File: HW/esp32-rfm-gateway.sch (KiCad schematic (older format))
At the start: 31 parts, among them J1 ph_1x2, J2 ph_1x2, J3 ph_1x3, J30 AntSMA, J4 ph_1x4, J5 ph_1x4, J6 ph_1x3, J7 ph_1x4, U1 ESP-WROOM-32, U2 BD48K30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

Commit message: Adds a new I2C connector, a LED for 5V indication, some SMD connections for a few free pins and labels
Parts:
- added J10, J11, J12, J13, J14: CS_1, CalinConnectors:SMD_Pins_1x1, symbol calin:CS_1
- added J8: ph_1x4, CalinConnectors:Pin_Header_Straight_1x04, symbol calin:CS_4
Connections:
- wire segments 134 -> 143
- no-connect marks 16 -> 12
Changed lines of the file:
@@
 Sheet 1 3
 Title "ESP32 RFM69/RFM9x Gateway"
-Date "2019-04-22"
-Rev "30"
+Date "2019-04-25"
+Rev "32"
 Comp "Calin Radoni"
 Comment1 ""
@@
 Connection ~ 5900 2900
 NoConn ~ 5900 1700
-NoConn ~ 5900 2300
-NoConn ~ 5900 2400
-NoConn ~ 5900 2500
 $Comp
 L calin:CS_5 J30
@@
 Text Label 7750 1400 0    50   ~ 0
 SDA
-NoConn ~ 5900 2800
 Text Label 5200 2800 0    50   ~ 0
 IO4
@@
 Text Label 8150 5150 0    50   ~ 0
 Reset
+$Comp
+L calin:CS_4 J8
+U 1 1 5CC3F23B
+P 9300 1250
+F 0 "J8" H 9300 1500 60  0000 C CNN
+F 1 "ph_1x4" V 9400 1250 50  0000 C CNN
+F 2 "CalinConnectors:Pin_Header_Straight_1x04" H 9300 1400 60  0001 C CNN
+F 3 "" H 9300 1400 60  0000 C CNN
+	1    9300 1250
+	1    0    0    -1
+$EndComp
+$Comp
+L power:GND #PWR0178
+U 1 1 5CC3F241
+P 9050 1200
+F 0 "#PWR0178" H 9050 950 50  0001 C CNN
+F 1 "GND" V 9050 1000 50  0000 C CNN
+F 2 "" H 9050 1200 50  0000 C CNN
+F 3 "" H 9050 1200 50  0000 C CNN
+	1    9050 1200
+	0    1    1    0
+$EndComp
+$Comp
+L power:+3V3 #PWR0179
+U 1 1 5CC3F247
+P 9050 1100
+F 0 "#PWR0179" H 9050 950 50  0001 C CNN
+F 1 "+3V3" V 9050 1300 50  0000 C CNN
+F 2 "" H 9050 1100 50  0000 C CNN
+F 3 "" H 9050 1100 50  0000 C CNN
+	1    9050 1100
+	0    -1   -1   0
+$EndComp
+Wire Wire Line
+	9150 1100 9050 1100
+Wire Wire Line
+	9150 1200 9050 1200
+Wire Wire Line
+	9150 1300 8650 1300
+Wire Wire Line
+	9150 1400 8650 1400
+Text Label 8750 1300 0    50   ~ 0
+SCL
+Text Label 8750 1400 0    50   ~ 0
+SDA
+$Comp
+L calin:CS_1 J10
+U 1 1 5CC44237
+P 9300 1900
+F 0 "J10" H 9400 1900 60  0000 L CNN
+F 1 "CS_1" H 9600 1900 50  0000 L CNN
+F 2 "CalinConnectors:SMD_Pins_1x1" H 9300 1900 60  0001 C CNN
+F 3 "" H 9300 1900 60  0000 C CNN
+	1    9300 1900
+	1    0    0    -1
+$EndComp
+$Comp
+L calin:CS_1 J11
+U 1 1 5CC442FF
+P 9300 2050
+F 0 "J11" H 9400 2050 60  0000 L CNN
+F 1 "CS_1" H 9600 2050 50  0000 L CNN
+F 2 "CalinConnectors:SMD_Pins_1x1" H 9300 2050 60  0001 C CNN
+F 3 "" H 9300 2050 60  0000 C CNN
+	1    9300 2050
+	1    0    0    -1
+$EndComp
+$Comp
+L calin:CS_1 J12
+U 1 1 5CC44353
+P 9300 2200
+F 0 "J12" H 9400 2200 60  0000 L CNN
+F 1 "CS_1" H 9600 2200 50  0000 L CNN
+F 2 "CalinConnectors:SMD_Pins_1x1" H 9300 2200 60  0001 C CNN
+F 3 "" H 9300 2200 60  0000 C CNN
+	1    9300 2200
+	1    0    0    -1
+$EndComp
+$Comp
+L calin:CS_1 J13
+U 1 1 5CC443A9
+P 9300 2350
+F 0 "J13" H 9400 2350 60  0000 L CNN
+F 1 "CS_1" H 9600 2350 50  0000 L CNN
+F 2 "CalinConnectors:SMD_Pins_1x1" H 9300 2350 60  0001 C CNN
+F 3 "" H 9300 2350 60  0000 C CNN
+	1    9300 2350
+	1    0    0    -1
+$EndComp
+$Comp
+L calin:CS_1 J14
+U 1 1 5CC44401
+P 9300 2500
+F 0 "J14" H 9400 2500 60  0000 L CNN
+F 1 "CS_1" H 9600 2500 50  0000 L CNN
+F 2 "CalinConnectors:SMD_Pins_1x1" H 9300 2500 60  0001 C CNN
+F 3 "" H 9300 2500 60  0000 C CNN
+	1    9300 2500
+	1    0    0    -1
+$EndComp
+Wire Wire Line
+	9150 1900 8650 1900
+Wire Wire Line
+	9150 2050 8650 2050
+Wire Wire Line
+	9150 2200 8650 2200
+Wire Wire Line
+	9150 2500 8650 2500
+$Comp
+L power:GND #PWR0180
+U 1 1 5CC64F5B
+P 9050 2350
+F 0 "#PWR0180" H 9050 2100 50  0001 C CNN
+F 1 "GND" V 9050 2150 50  0000 C CNN
+F 2 "" H 9050 2350 50  0000 C CNN
+F 3 "" H 9050 2350 50  0000 C CNN
+	1    9050 2350
+	0    1    1    0
+$EndComp
+Wire Wire Line
+	9150 2350 9050 2350
+Text Label 8750 2500 0    50   ~ 0
+IO4
+Text Label 8750 2200 0    50   ~ 0
+IO5
+Text Label 8750 2050 0    50   ~ 0
+IO18
+Text Label 8750 1900 0    50   ~ 0
+IO19
 $EndSCHEMATC

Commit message: Updates components to add manufacturer, part number, ... fields. Also checked some values.
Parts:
- C1, C2, C30, C32, C4, C5, C6: symbol Device:C -> calin:C; characteristics (none) -> 100 nF / 50V / X7R; manufacturer (none) -> Samsung; package (none) -> 0805; part-number (none) -> CL21B104KBCNNNC
- C3, C31: symbol Device:C -> calin:C; characteristics (none) -> 10 µF / 6,3 V; manufacturer (none) -> Samsung; package (none) -> 0805; part-number (none) -> CL21B106KQQNNNE
- H1, H2, H3, H4, J10, J11, J12, J13, J14: Notes (none) -> DNP; Variant (none) -> pcb
- J1, J2, J7: Notes (none) -> DNP; Variant (none) -> test
- R1: characteristics (none) -> 10k; manufacturer (none) -> Vishay; package (none) -> 0805; part-number (none) -> CRCW080510K0FKEA
- R2: characteristics (none) -> 330; manufacturer (none) -> Vishay; package (none) -> 0805; part-number (none) -> CRCW0805330RFKTABC
- R3, R4: characteristics (none) -> 2k; manufacturer (none) -> Panasonic; package (none) -> 0805; part-number (none) -> ERJ6ENF2001V
- SYM2, SYM5: Notes (none) -> DNP; Variant (none) -> pcb; part-number (none) -> DNP
- U1: characteristics (none) -> *; manufacturer (none) -> Espressif; package (none) -> *; part-number (none) -> ESP32-WROOM-32
- U2: Notes (none) -> DNP; Variant (none) -> test; characteristics (none) -> Standard CMOS Voltage Detector IC 3.0V; manufacturer (none) -> ROHM Semiconductor; package (none) -> SSOP3 (SOT23-3); part-number (none) -> BD49K30
- U30: characteristics (none) -> *; manufacturer (none) -> HOPERF; package (none) -> *; part-number (none) -> RFM69HCW

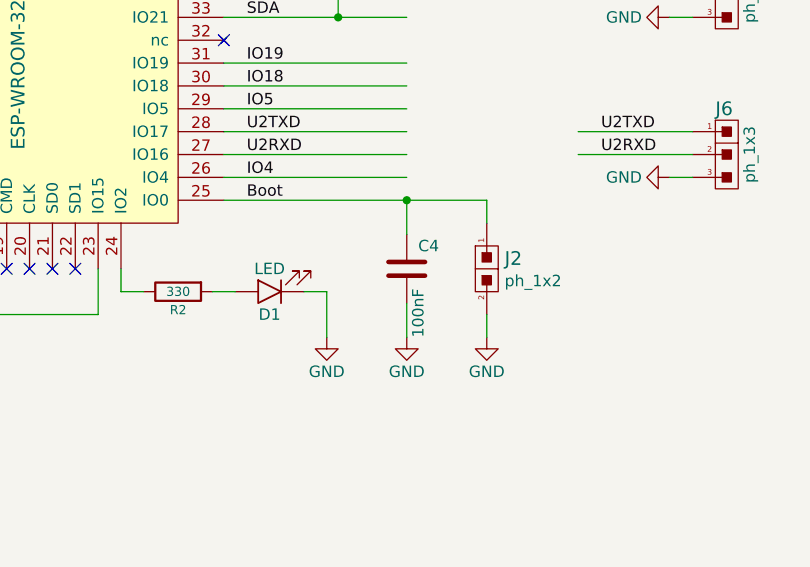
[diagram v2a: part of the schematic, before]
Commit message: Changes C4 to NC to prevent unwanted boot to Download mode and removes keepout area from under the ESP32 module.
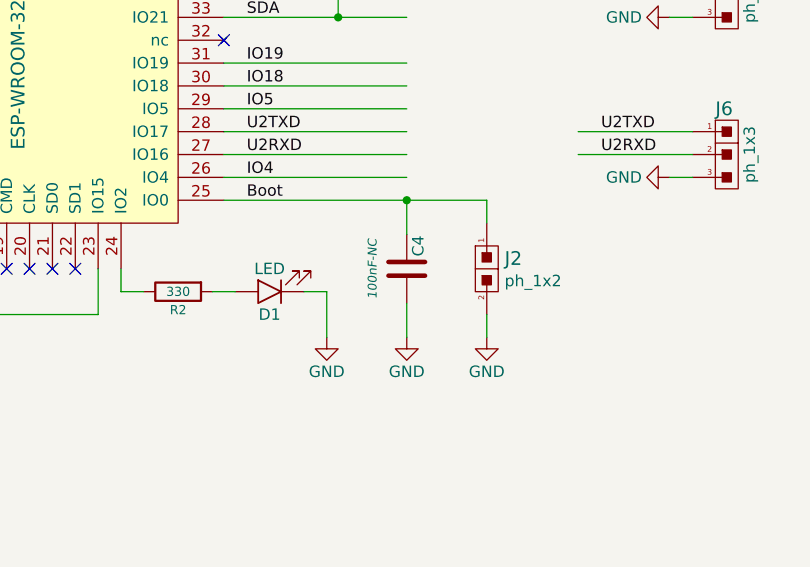
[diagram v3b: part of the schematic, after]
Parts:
- C4: value 100nF -> 100nF-NC; characteristics 100 nF / 50V / X7R -> *; manufacturer Samsung -> *; part-number CL21B104KBCNNNC -> DNP
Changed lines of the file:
@@
 Title "ESP32 RFM69/RFM9x Gateway"
 Date "2019-05-02"
-Rev "33"
+Rev "34"
 Comp "Calin Radoni"
 Comment1 ""
@@
 U 1 1 5B37F59B
 P 5900 3200
-F 0 "C4" H 5950 3300 50  0000 L CNN
-F 1 "100nF" V 5950 2900 50  0000 L CNN
+F 0 "C4" V 5950 3300 50  0000 C CNN
+F 1 "100nF-NC" V 5750 3200 39  0000 C CIN
 F 2 "CalinGeneric:C0805HS" H 5938 3050 50  0001 C CNN
 F 3 "" H 5900 3200 50  0000 C CNN
-F 4 "100 nF / 50V / X7R" H 0   0   50  0001 C CNN "characteristics"
-F 5 "Samsung" H 0   0   50  0001 C CNN "manufacturer"
+F 4 "*" H 0   0   50  0001 C CNN "characteristics"
+F 5 "*" H 0   0   50  0001 C CNN "manufacturer"
 F 6 "0805" H 0   0   50  0001 C CNN "package"
-F 7 "CL21B104KBCNNNC" H 0   0   50  0001 C CNN "part-number"
+F 7 "DNP" H 0   0   50  0001 C CNN "part-number"
 	1    5900 3200
 	1    0    0    -1

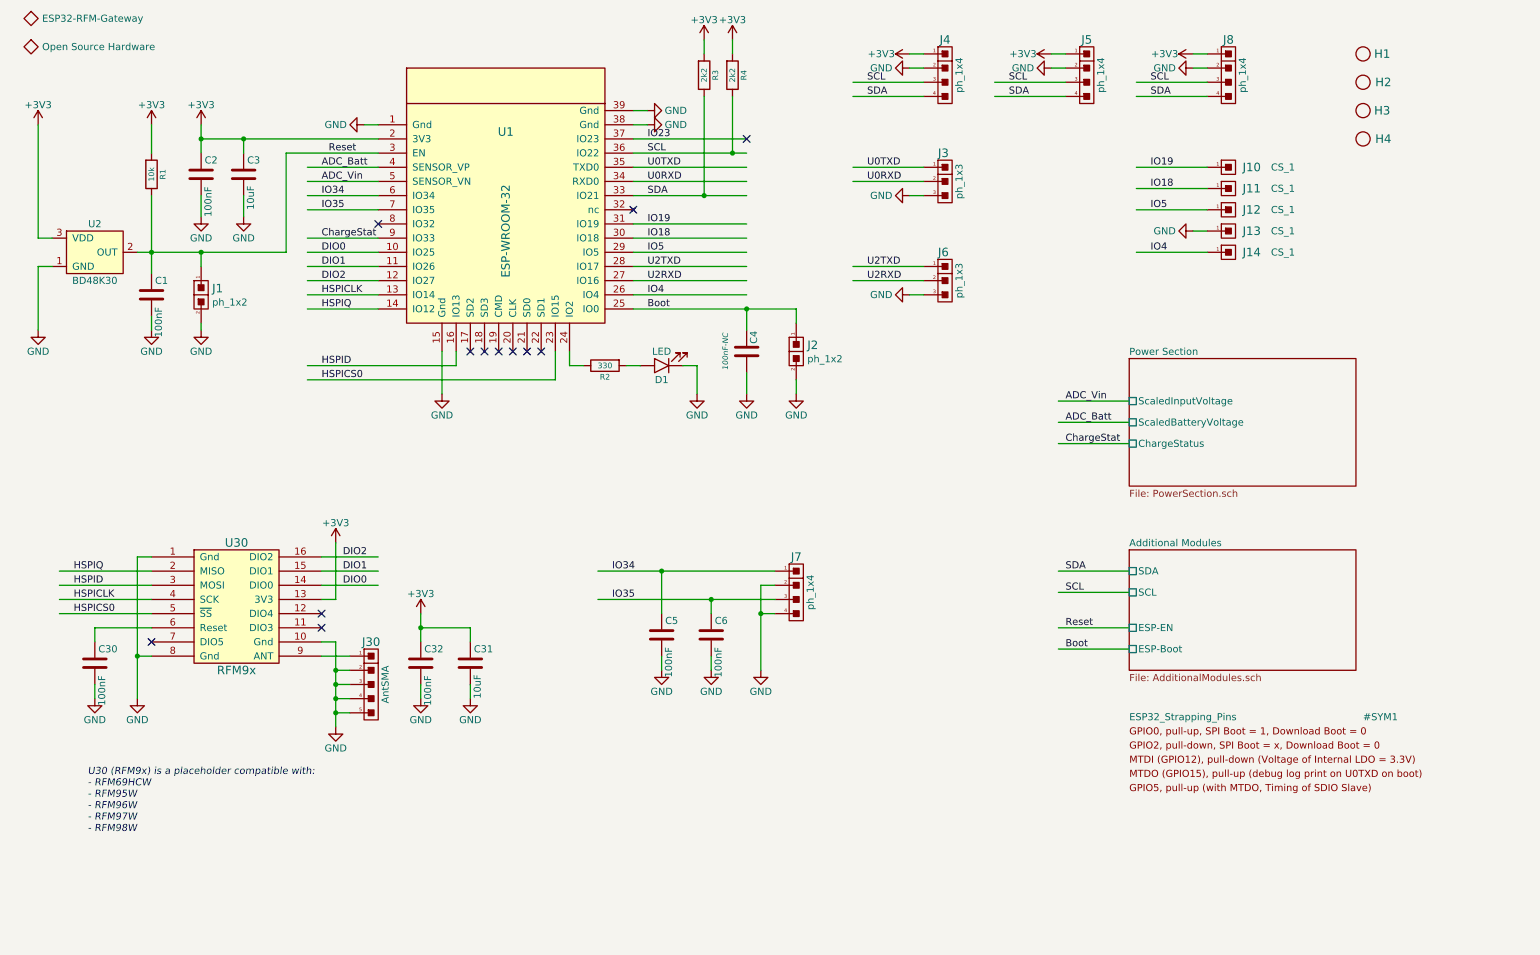
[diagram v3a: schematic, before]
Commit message: Connects the LEDs straight to ESP32, removing the LED driver.
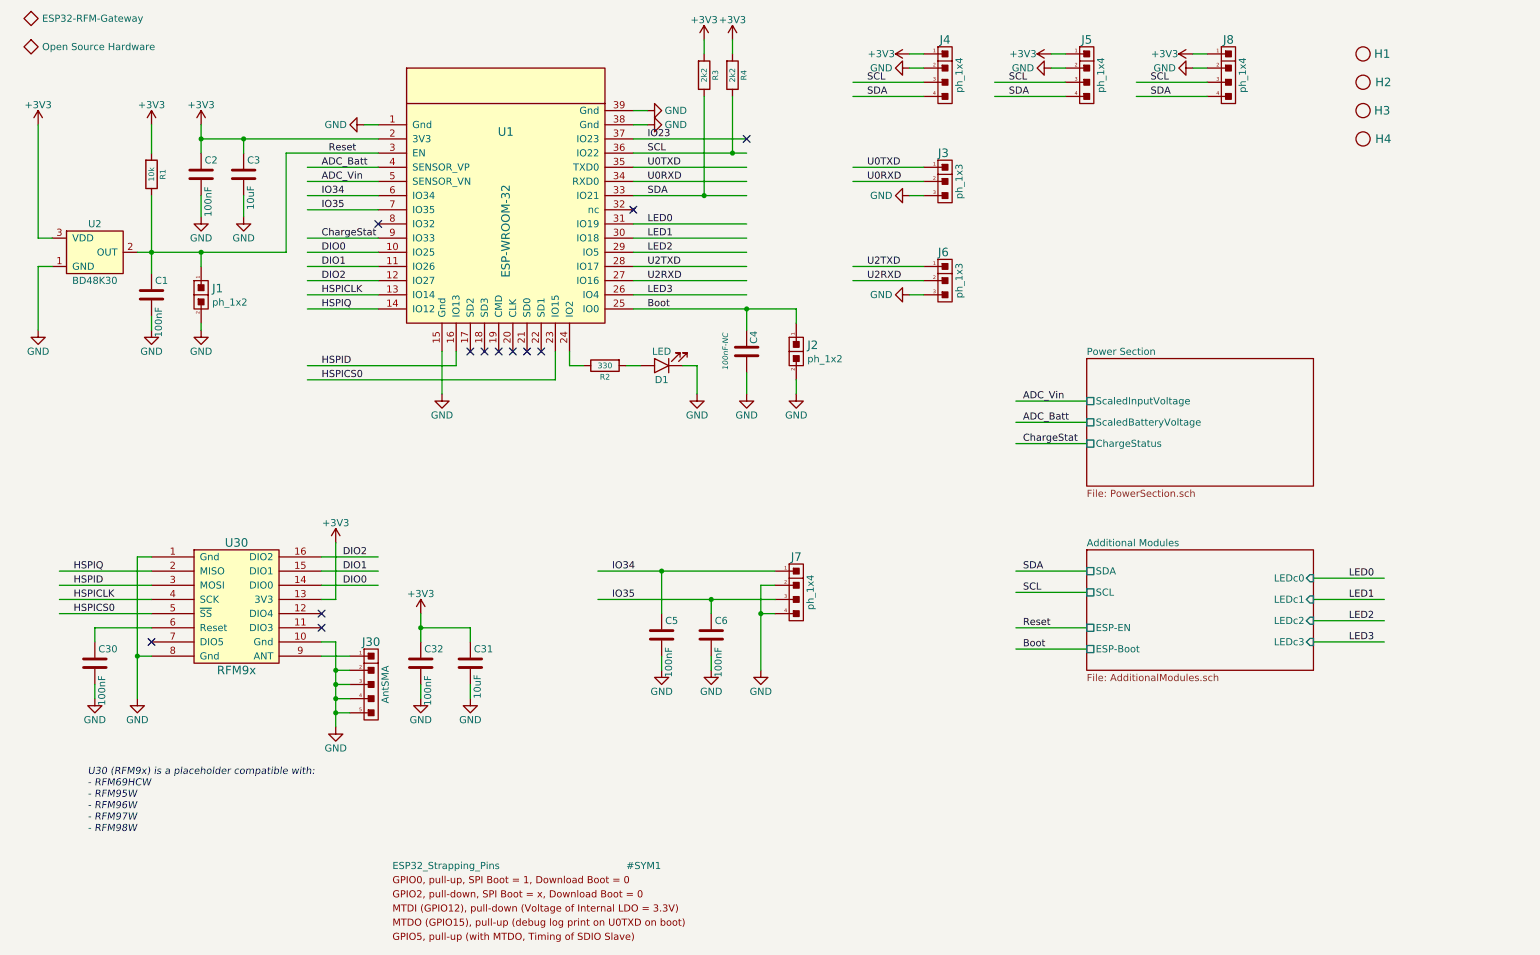
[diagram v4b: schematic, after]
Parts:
- removed J10, J11, J12, J13, J14: CS_1, CalinConnectors:SMD_Pins_1x1, symbol calin:CS_1
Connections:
- net labels added: LED0, LED1, LED2, LED3
- net labels removed: IO18, IO19, IO4, IO5
- wire segments 143 -> 142
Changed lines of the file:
@@
 Title "ESP32 RFM69/RFM9x Gateway"
 Date "2019-05-02"
-Rev "34"
+Rev "35"
 Comp "Calin Radoni"
 Comment1 ""
@@
 L calin:ESP32_Strapping_Pins #SYM1
 U 1 1 5C6162CE
-P 9400 6050
-F 0 "#SYM1" H 10250 6350 50  0000 L TNN
-F 1 "ESP32_Strapping_Pins" H 8600 6350 50  0000 L TNN
-F 2 "" H 9200 5850 50  0001 C CNN
-F 3 "" H 9200 5850 50  0001 C CNN
-	1    9400 6050
+P 4200 7100
+F 0 "#SYM1" H 5050 7400 50  0000 L TNN
+F 1 "ESP32_Strapping_Pins" H 3400 7400 50  0000 L TNN
+F 2 "" H 4000 6900 50  0001 C CNN
+F 3 "" H 4000 6900 50  0001 C CNN
+	1    4200 7100
 	1    0    0    -1
 $EndComp
@@
 	5100 2400 5900 2400
 Text Label 5200 2500 0    50   ~ 0
-IO5
+LED2
 Text Label 5200 2300 0    50   ~ 0
-IO19
+LED0
 Text Label 5200 2400 0    50   ~ 0
-IO18
+LED1
 Wire Wire Line
 	5100 1700 5900 1700
@@
 SDA
 Text Label 5200 2800 0    50   ~ 0
-IO4
+LED3
 Text Label 2900 2400 0    50   ~ 0
 ChargeStat
@@
 $EndComp
 $Sheet
-S 8600 3250 1600 900
+S 8300 3250 1600 900
 U 5CBFFED5
 F0 "Power Section" 50
 F1 "PowerSection.sch" 50
-F2 "ScaledInputVoltage" U L 8600 3550 50
-F3 "ScaledBatteryVoltage" U L 8600 3700 50
-F4 "ChargeStatus" U L 8600 3850 50
+F2 "ScaledInputVoltage" U L 8300 3550 50
+F3 "ScaledBatteryVoltage" U L 8300 3700 50
+F4 "ChargeStatus" U L 8300 3850 50
 $EndSheet
 $Comp
@@
 Connection ~ 5650 4950
 $Sheet
-S 8600 4600 1600 850
+S 8300 4600 1600 850
 U 5CCB086C
 F0 "Additional Modules" 50
 F1 "AdditionalModules.sch" 50
-F2 "SDA" U L 8600 4750 50
-F3 "SCL" U L 8600 4900 50
-F4 "ESP-EN" U L 8600 5150 50
-F5 "ESP-Boot" U L 8600 5300 50
+F2 "SDA" U L 8300 4750 50
+F3 "SCL" U L 8300 4900 50
+F4 "ESP-EN" U L 8300 5150 50
+F5 "ESP-Boot" U L 8300 5300 50
+F6 "LEDc0" I R 9900 4800 50
+F7 "LEDc1" I R 9900 4950 50
+F8 "LEDc2" I R 9900 5100 50
+F9 "LEDc3" I R 9900 5250 50
 $EndSheet
-Text Label 8150 4750 0    50   ~ 0
+Text Label 7850 4750 0    50   ~ 0
 SDA
-Text Label 8150 4900 0    50   ~ 0
+Text Label 7850 4900 0    50   ~ 0
 SCL
 Text Notes 1250 6600 0    50   Italic 0
 U30 (RFM9x) is a placeholder compatible with:\n- RFM69HCW\n- RFM95W\n- RFM96W\n- RFM97W\n- RFM98W
-Text Label 8150 3700 0    50   ~ 0
+Text Label 7850 3700 0    50   ~ 0
 ADC_Batt
-Text Label 8150 3550 0    50   ~ 0
+Text Label 7850 3550 0    50   ~ 0
 ADC_Vin
-Text Label 8150 3850 0    50   ~ 0
+Text Label 7850 3850 0    50   ~ 0
 ChargeStat
 Wire Wire Line
-	8600 3550 8100 3550
-Wire Wire Line
-	8600 3700 8100 3700
-Wire Wire Line
-	8600 3850 8100 3850
-Wire Wire Line
-	8600 4750 8100 4750
-Wire Wire Line
-	8600 4900 8100 4900
-Wire Wire Line
-	8600 5150 8100 5150
-Wire Wire Line
-	8600 5300 8100 5300
-Text Label 8150 5300 0    50   ~ 0
+	8300 3550 7800 3550
+Wire Wire Line
+	8300 3700 7800 3700
+Wire Wire Line
+	8300 3850 7800 3850
+Wire Wire Line
+	8300 4750 7800 4750
+Wire Wire Line
+	8300 4900 7800 4900
+Wire Wire Line
+	8300 5150 7800 5150
+Wire Wire Line
+	8300 5300 7800 5300
+Text Label 7850 5300 0    50   ~ 0
 Boot
-Text Label 8150 5150 0    50   ~ 0
+Text Label 7850 5150 0    50   ~ 0
 Reset
 $Comp
@@
 Text Label 8750 1400 0    50   ~ 0
 SDA
-$Comp
-L calin:CS_1 J10
-U 1 1 5CC44237
-P 9300 1900
-F 0 "J10" H 9400 1900 60  0000 L CNN
-F 1 "CS_1" H 9600 1900 50  0000 L CNN
-F 2 "CalinConnectors:SMD_Pins_1x1" H 9300 1900 60  0001 C CNN
-F 3 "" H 9300 1900 60  0000 C CNN
-F 4 "DNP" H 0   0   50  0001 C CNN "Notes"
-F 5 "pcb" H 0   0   50  0001 C CNN "Variant"
-	1    9300 1900
-	1    0    0    -1
-$EndComp
-$Comp
-L calin:CS_1 J11
-U 1 1 5CC442FF
-P 9300 2050
-F 0 "J11" H 9400 2050 60  0000 L CNN
-F 1 "CS_1" H 9600 2050 50  0000 L CNN
-F 2 "CalinConnectors:SMD_Pins_1x1" H 9300 2050 60  0001 C CNN
-F 3 "" H 9300 2050 60  0000 C CNN
-F 4 "DNP" H 0   0   50  0001 C CNN "Notes"
-F 5 "pcb" H 0   0   50  0001 C CNN "Variant"
-	1    9300 2050
-	1    0    0    -1
-$EndComp
-$Comp
-L calin:CS_1 J12
-U 1 1 5CC44353
-P 9300 2200
-F 0 "J12" H 9400 2200 60  0000 L CNN
-F 1 "CS_1" H 9600 2200 50  0000 L CNN
-F 2 "CalinConnectors:SMD_Pins_1x1" H 9300 2200 60  0001 C CNN
-F 3 "" H 9300 2200 60  0000 C CNN
-F 4 "DNP" H 0   0   50  0001 C CNN "Notes"
-F 5 "pcb" H 0   0   50  0001 C CNN "Variant"
-	1    9300 2200
-	1    0    0    -1
-$EndComp
-$Comp
-L calin:CS_1 J13
-U 1 1 5CC443A9
-P 9300 2350
-F 0 "J13" H 9400 2350 60  0000 L CNN
-F 1 "CS_1" H 9600 2350 50  0000 L CNN
-F 2 "CalinConnectors:SMD_Pins_1x1" H 9300 2350 60  0001 C CNN
-F 3 "" H 9300 2350 60  0000 C CNN
-F 4 "DNP" H 0   0   50  0001 C CNN "Notes"
-F 5 "pcb" H 0   0   50  0001 C CNN "Variant"
-	1    9300 2350
-	1    0    0    -1
-$EndComp
-$Comp
-L calin:CS_1 J14
-U 1 1 5CC44401
-P 9300 2500
-F 0 "J14" H 9400 2500 60  0000 L CNN
-F 1 "CS_1" H 9600 2500 50  0000 L CNN
-F 2 "CalinConnectors:SMD_Pins_1x1" H 9300 2500 60  0001 C CNN
-F 3 "" H 9300 2500 60  0000 C CNN
-F 4 "DNP" H 0   0   50  0001 C CNN "Notes"
-F 5 "pcb" H 0   0   50  0001 C CNN "Variant"
-	1    9300 2500
-	1    0    0    -1
-$EndComp
-Wire Wire Line
-	9150 1900 8650 1900
-Wire Wire Line
-	9150 2050 8650 2050
-Wire Wire Line
-	9150 2200 8650 2200
-Wire Wire Line
-	9150 2500 8650 2500
-$Comp
-L power:GND #PWR0180
-U 1 1 5CC64F5B
-P 9050 2350
-F 0 "#PWR0180" H 9050 2100 50  0001 C CNN
-F 1 "GND" V 9050 2150 50  0000 C CNN
-F 2 "" H 9050 2350 50  0000 C CNN
-F 3 "" H 9050 2350 50  0000 C CNN
-	1    9050 2350
-	0    1    1    0
-$EndComp
-Wire Wire Line
-	9150 2350 9050 2350
-Text Label 8750 2500 0    50   ~ 0
-IO4
-Text Label 8750 2200 0    50   ~ 0
-IO5
-Text Label 8750 2050 0    50   ~ 0
-IO18
-Text Label 8750 1900 0    50   ~ 0
-IO19
+Text Label 10150 5250 0    50   ~ 0
+LED3
+Text Label 10150 5100 0    50   ~ 0
+LED2
+Text Label 10150 4950 0    50   ~ 0
+LED1
+Text Label 10150 4800 0    50   ~ 0
+LED0
+Wire Wire Line
+	9900 4800 10400 4800
+Wire Wire Line
+	9900 4950 10400 4950
+Wire Wire Line
+	9900 5100 10400 5100
+Wire Wire Line
+	9900 5250 10400 5250
 $EndSCHEMATC
